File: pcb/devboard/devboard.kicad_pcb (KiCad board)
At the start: 2 copper layers, 8 parts, among them J1 USB4110GFA, J3 Conn_01x16_Pin, J4 Conn_01x16_Pin, SW1 PTS526_SM15_SMTR2_LFS, SW2 PTS526_SM15_SMTR2_LFS, U1 ESP32-S3-MINI-1U, U2 IP4234CZ6, U3 ADP2108AUJ-3.3

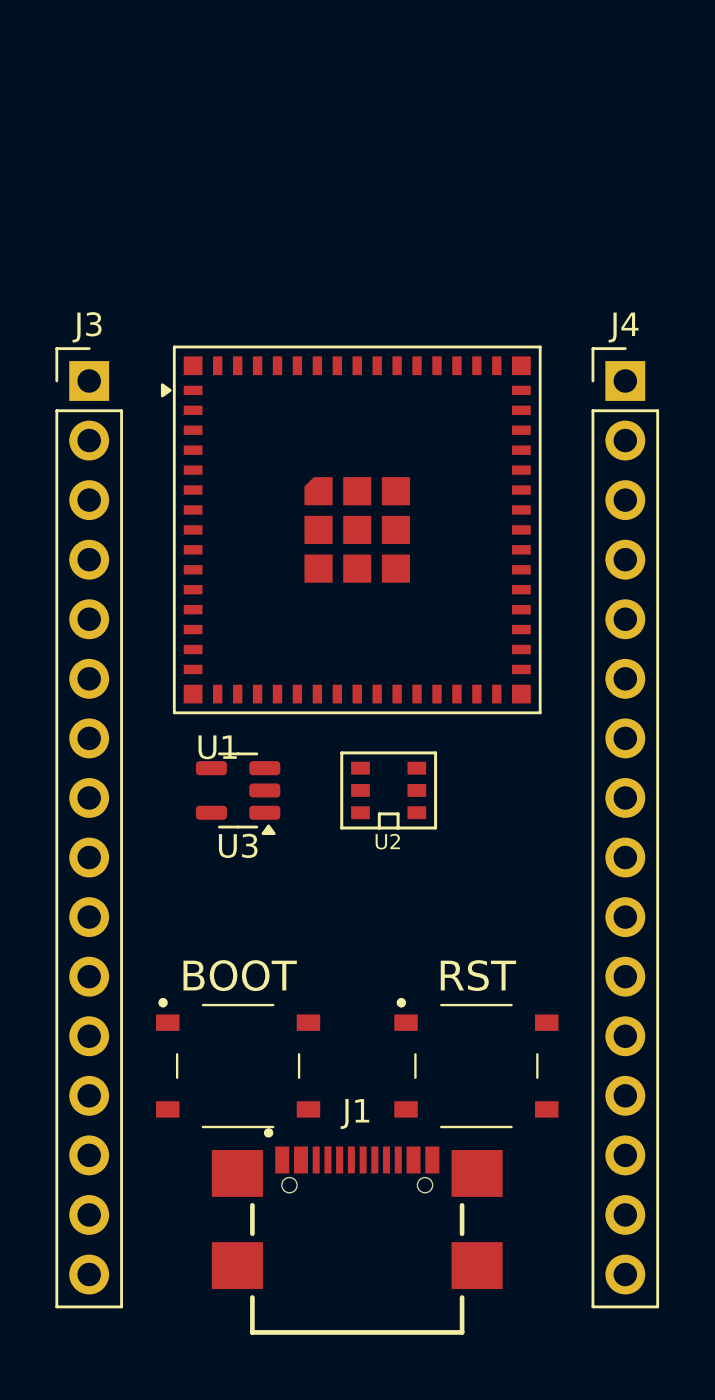
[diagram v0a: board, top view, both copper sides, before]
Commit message: connecting all remaining IOs
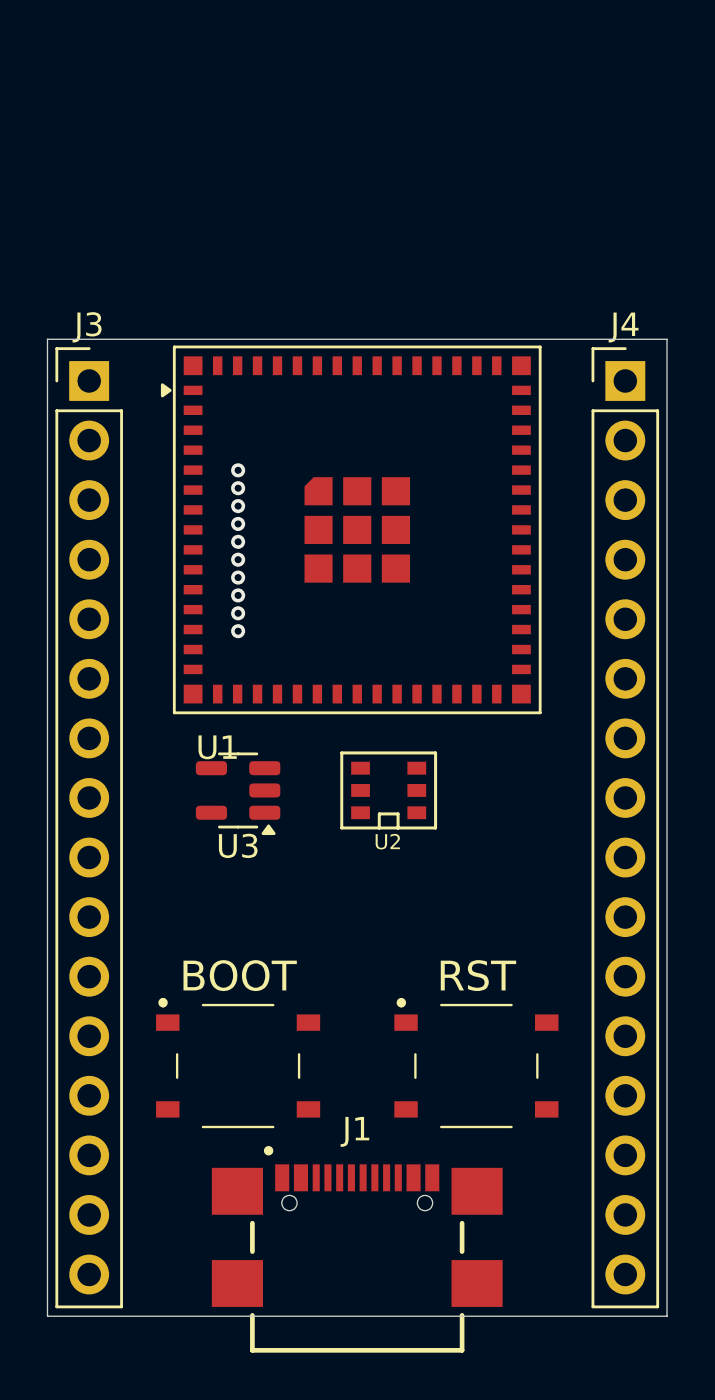
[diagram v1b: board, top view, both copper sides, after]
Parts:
- moved J1 0.76 mm to (151.1, 101.1)
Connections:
- net IO14 renamed 14
- net IO15 renamed 15
- net IO16 renamed 16
- J4 pad 10: unconnected-(J4-Pin_10-Pad10) -> 8
- J4 pad 11: unconnected-(J4-Pin_11-Pad11) -> 9
- J4 pad 12: unconnected-(J4-Pin_12-Pad12) -> 33
- J4 pad 13: unconnected-(J4-Pin_13-Pad13) -> 34
- J4 pad 14: unconnected-(J4-Pin_14-Pad14) -> 35
- J4 pad 15: unconnected-(J4-Pin_15-Pad15) -> 36
- J4 pad 16: unconnected-(J4-Pin_16-Pad16) -> 37
- J4 pad 3: unconnected-(J4-Pin_3-Pad3) -> 1
- J4 pad 4: unconnected-(J4-Pin_4-Pad4) -> 2
- J4 pad 5: unconnected-(J4-Pin_5-Pad5) -> 3
- J4 pad 6: unconnected-(J4-Pin_6-Pad6) -> 4
- J4 pad 7: unconnected-(J4-Pin_7-Pad7) -> 5
- J4 pad 8: unconnected-(J4-Pin_8-Pad8) -> 6
- J4 pad 9: unconnected-(J4-Pin_9-Pad9) -> 7
- U1 pad 10: unconnected-(U1-IO6-Pad10) -> 6
- U1 pad 11: unconnected-(U1-IO7-Pad11) -> 7
- U1 pad 12: unconnected-(U1-IO8-Pad12) -> 8
- U1 pad 13: unconnected-(U1-IO9-Pad13) -> 9
- U1 pad 28: unconnected-(U1-IO33-Pad28) -> 33
- U1 pad 29: unconnected-(U1-IO34-Pad29) -> 34
- U1 pad 31: unconnected-(U1-IO35-Pad31) -> 35
- U1 pad 32: unconnected-(U1-IO36-Pad32) -> 36
- U1 pad 33: unconnected-(U1-IO37-Pad33) -> 37
- U1 pad 5: unconnected-(U1-IO1-Pad5) -> 1
- U1 pad 6: unconnected-(U1-IO2-Pad6) -> 2
- U1 pad 7: unconnected-(U1-IO3-Pad7) -> 3
- U1 pad 8: unconnected-(U1-IO4-Pad8) -> 4
- U1 pad 9: unconnected-(U1-IO5-Pad9) -> 5
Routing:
- net (no net): vias 0 -> 10
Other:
- board outline added: 26.4 x 41.7 mm

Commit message: adding mouser part number to all parts
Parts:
- added R1: 5k1, Resistor_SMD:R_0402_1005Metric, F.Cu at (148.0, 54.0)
- added R2: 5k1, Resistor_SMD:R_0402_1005Metric, F.Cu at (148.0, 56.0)
- added R3: 10k, Resistor_SMD:R_0402_1005Metric, F.Cu at (145.0, 54.0)
- added R4: 10k, Resistor_SMD:R_0402_1005Metric, F.Cu at (145.0, 56.0)
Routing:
- net GND: track 0.00 -> 33.8 mm
- net BTN_BOOT: track 0.00 -> 5.31 mm
- net VCC_3.3V: track 0.00 -> 4.61 mm

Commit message: designed pcb
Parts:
- added C1: 4.7uF, Capacitor_SMD:C_0603_1608Metric, F.Cu at (151.1, 83.6)
- added C2: 10uF, Capacitor_SMD:C_0805_2012Metric, F.Cu at (147.8, 83.3)
- added C3: 0u1F, Capacitor_SMD:C_0402_1005Metric, F.Cu at (159.3, 99.5)
- added C4: 0u1F, Capacitor_SMD:C_0402_1005Metric, F.Cu at (143.0, 99.5)
- added C5: 0u1F, Capacitor_SMD:C_0402_1005Metric, F.Cu at (142.2, 67.3)
- added L1: 1uH, Inductor_SMD:L_0805_2012Metric, F.Cu at (146.8, 86.4)
- moved R1 50.0 mm to (159.8, 102.6), turned to 90 degrees
- moved R2 47.8 mm to (158.8, 102.6), turned to 90 degrees
- moved R3 43.1 mm to (151.9, 96.5), turned to -90 degrees
- moved R4 40.9 mm to (150.4, 96.5), turned to -90 degrees
- moved U2 4.83 mm to (157.2, 84.3)
- moved U3 4.76 mm to (149.9, 86.4)
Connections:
- J4 pad 12: 33 -> 37
- J4 pad 13: 34 -> 36
- J4 pad 15: 36 -> 34
- J4 pad 16: 37 -> GND
- U1 pad 28: 33 -> unconnected-(U1-IO33-Pad28)
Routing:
- net GND: track 33.8 -> 177.6 mm, vias 0 -> 5
- net BTN_RST: track 0.00 -> 61.3 mm, vias 0 -> 2
- net VCC_5V: track 0.00 -> 48.8 mm, vias 0 -> 5
- net BTN_BOOT: track 5.31 -> 48.1 mm, vias 0 -> 2
- net VCC_3.3V: track 4.61 -> 46.4 mm, vias 0 -> 2
- net EXT_D+: track 0.00 -> 38.1 mm, vias 0 -> 1
- net EXT_D-: track 0.00 -> 35.9 mm, vias 0 -> 1
- net 9: track 0.00 -> 26.3 mm, vias 0 -> 1
- net 34: track 0.00 -> 24.8 mm
- net 8: track 0.00 -> 24.4 mm, vias 0 -> 1
- net 7: track 0.00 -> 23.6 mm, vias 0 -> 1
- net 6: track 0.00 -> 22.8 mm, vias 0 -> 1
- net 35: track 0.00 -> 22.7 mm
- net 5: track 0.00 -> 22.0 mm, vias 0 -> 1
- net 4: track 0.00 -> 21.7 mm, vias 0 -> 1
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
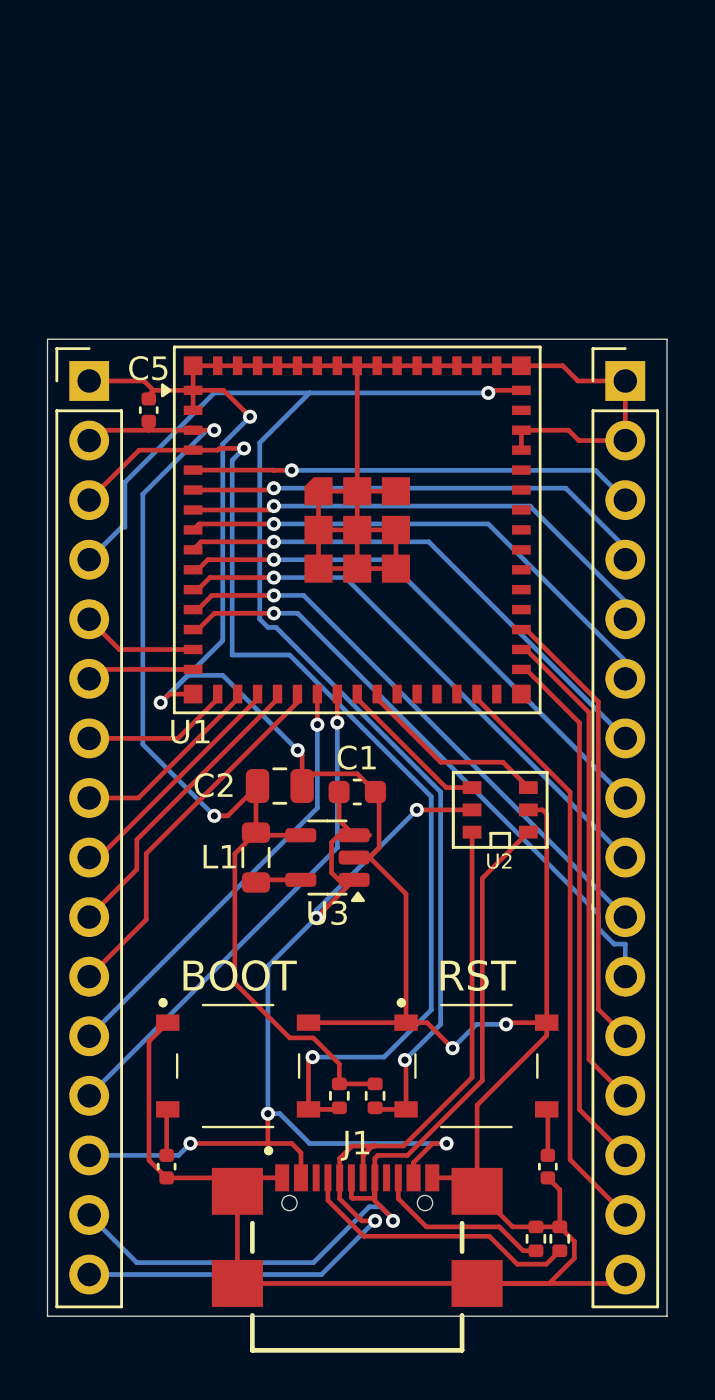
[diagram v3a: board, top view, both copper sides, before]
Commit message: changing pinout to more gnd
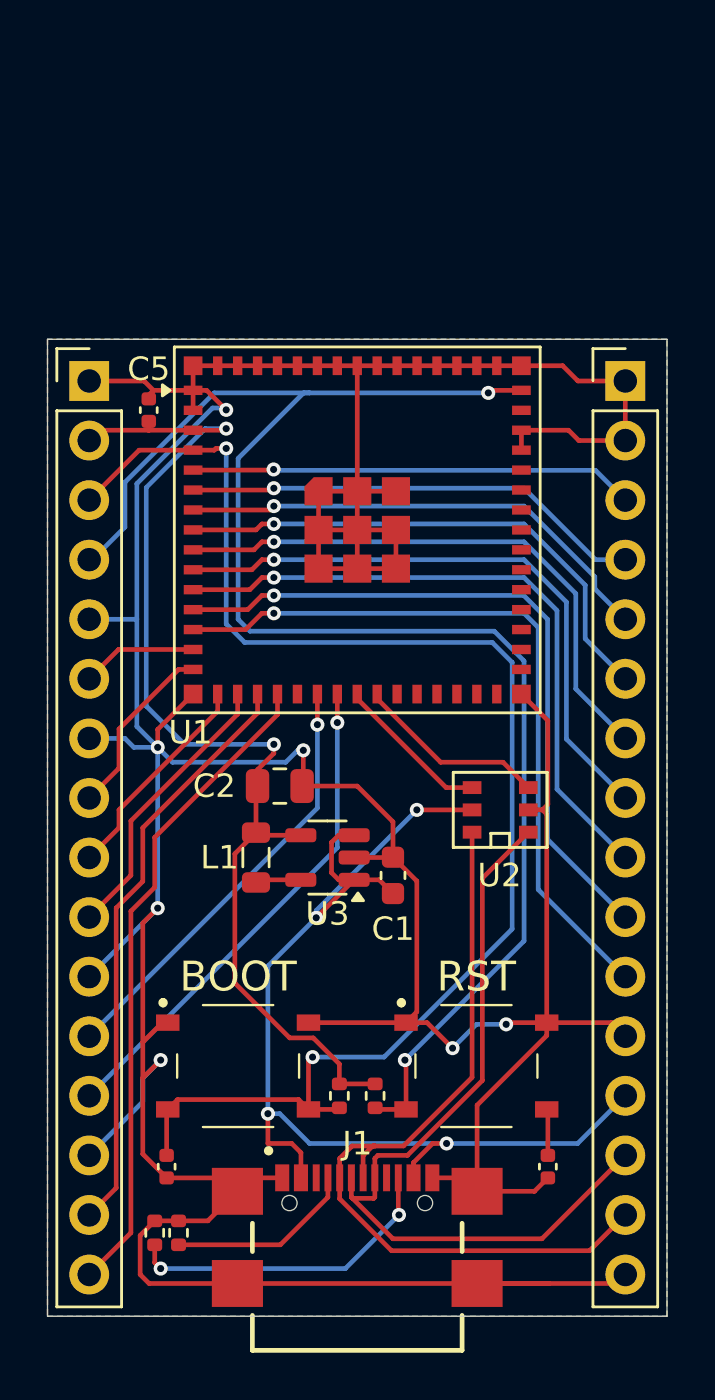
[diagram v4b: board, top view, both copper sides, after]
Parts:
- moved R1 16.3 mm to (143.5, 102.4)
- moved R2 16.3 mm to (142.5, 102.4)
- moved C1 3.87 mm to (152.7, 87.1), turned to 90 degrees
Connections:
- J3 pad 10: 15 -> SCK
- J3 pad 11: 16 -> GND
- J3 pad 14: VCC_5V -> GND
- J3 pad 15: EXT_D+ -> 14
- J3 pad 16: EXT_D- -> 15
- J3 pad 5: CS -> GND
- J3 pad 6: MOSI -> CS
- J3 pad 7: MISO -> GND
- J3 pad 8: SCK -> MOSI
- J3 pad 9: 14 -> MISO
- J4 pad 12: 37 -> GND
- J4 pad 13: 36 -> VCC_5V
- J4 pad 14: 35 -> EXT_D+
- J4 pad 15: 34 -> EXT_D-
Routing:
- net GND: track 177.6 -> 216.0 mm, vias 5 -> 7
- net 34: track 24.8 -> 0.00 mm
- net 35: track 22.7 -> 0.00 mm
- net 36: track 21.0 -> 0.00 mm
- net 37: track 19.3 -> 0.00 mm
- net 16: track 15.7 -> 0.00 mm
- net 14: track 10.2 -> 25.2 mm
- net 15: track 13.3 -> 28.1 mm
- net BTN_BOOT: track 48.1 -> 61.2 mm
- net BTN_RST: track 61.3 -> 71.1 mm
- net Net-(J1-CC2): track 7.68 -> 13.8 mm, vias 0 -> 2
- net 8: track 24.4 -> 29.9 mm
- net 9: track 26.3 -> 31.7 mm
- net 7: track 23.6 -> 28.1 mm
- net Net-(J1-CC1): track 12.2 -> 8.04 mm
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- added copper zone on B.Cu, net GND
- added copper zone on F.Cu, net GND

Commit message: adding GND vias, creating gerber files
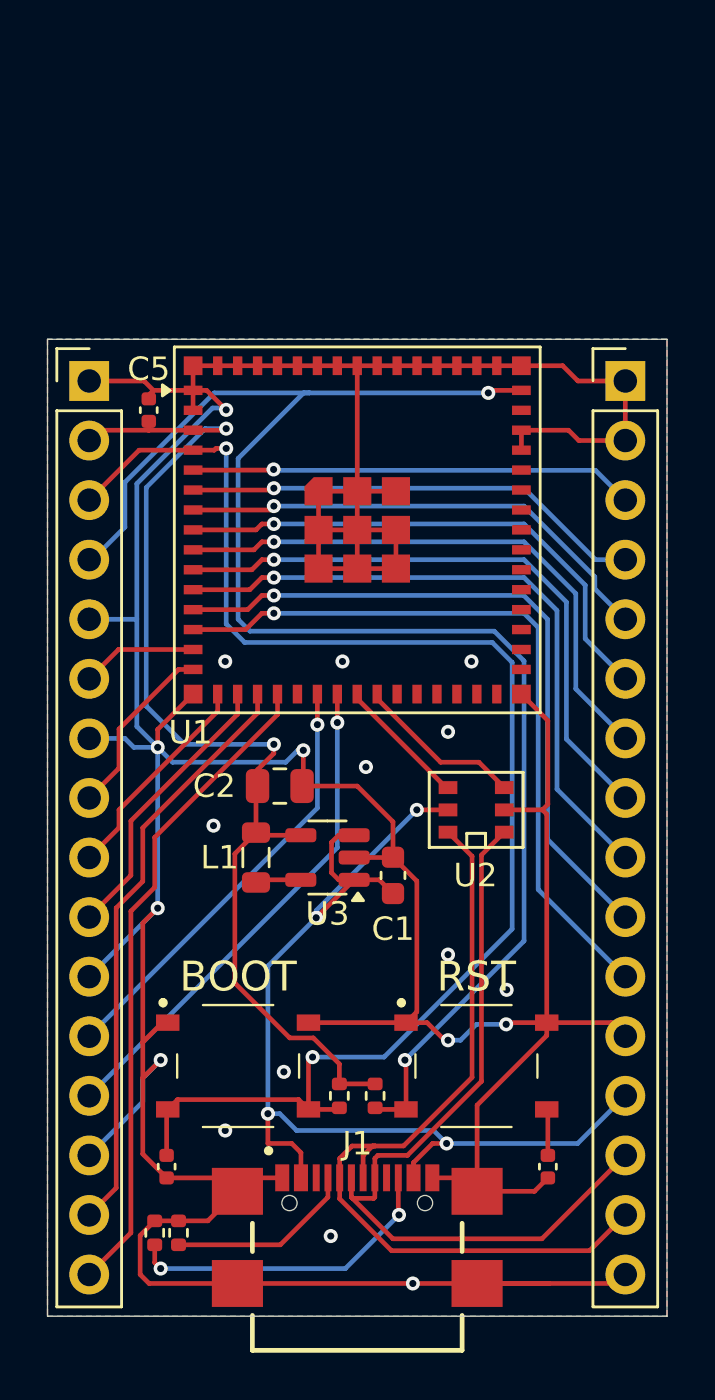
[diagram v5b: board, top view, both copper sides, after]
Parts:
- moved U2 1.03 mm to (156.2, 84.3)
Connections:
- U1 pad 20: 16 -> unconnected-(U1-IO16-Pad20)
- U1 pad 29: 34 -> unconnected-(U1-IO34-Pad29)
- U1 pad 31: 35 -> unconnected-(U1-IO35-Pad31)
- U1 pad 32: 36 -> unconnected-(U1-IO36-Pad32)
- U1 pad 33: 37 -> unconnected-(U1-IO37-Pad33)
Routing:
- net D-: track 6.67 -> 5.64 mm
- net VCC_5V: track 48.5 -> 47.5 mm
- net D+: track 8.22 -> 7.19 mm
- net GND: track 216.0 -> 216.8 mm, vias 7 -> 19
